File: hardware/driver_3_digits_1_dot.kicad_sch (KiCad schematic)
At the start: 12 parts, among them U4 HV5622PG

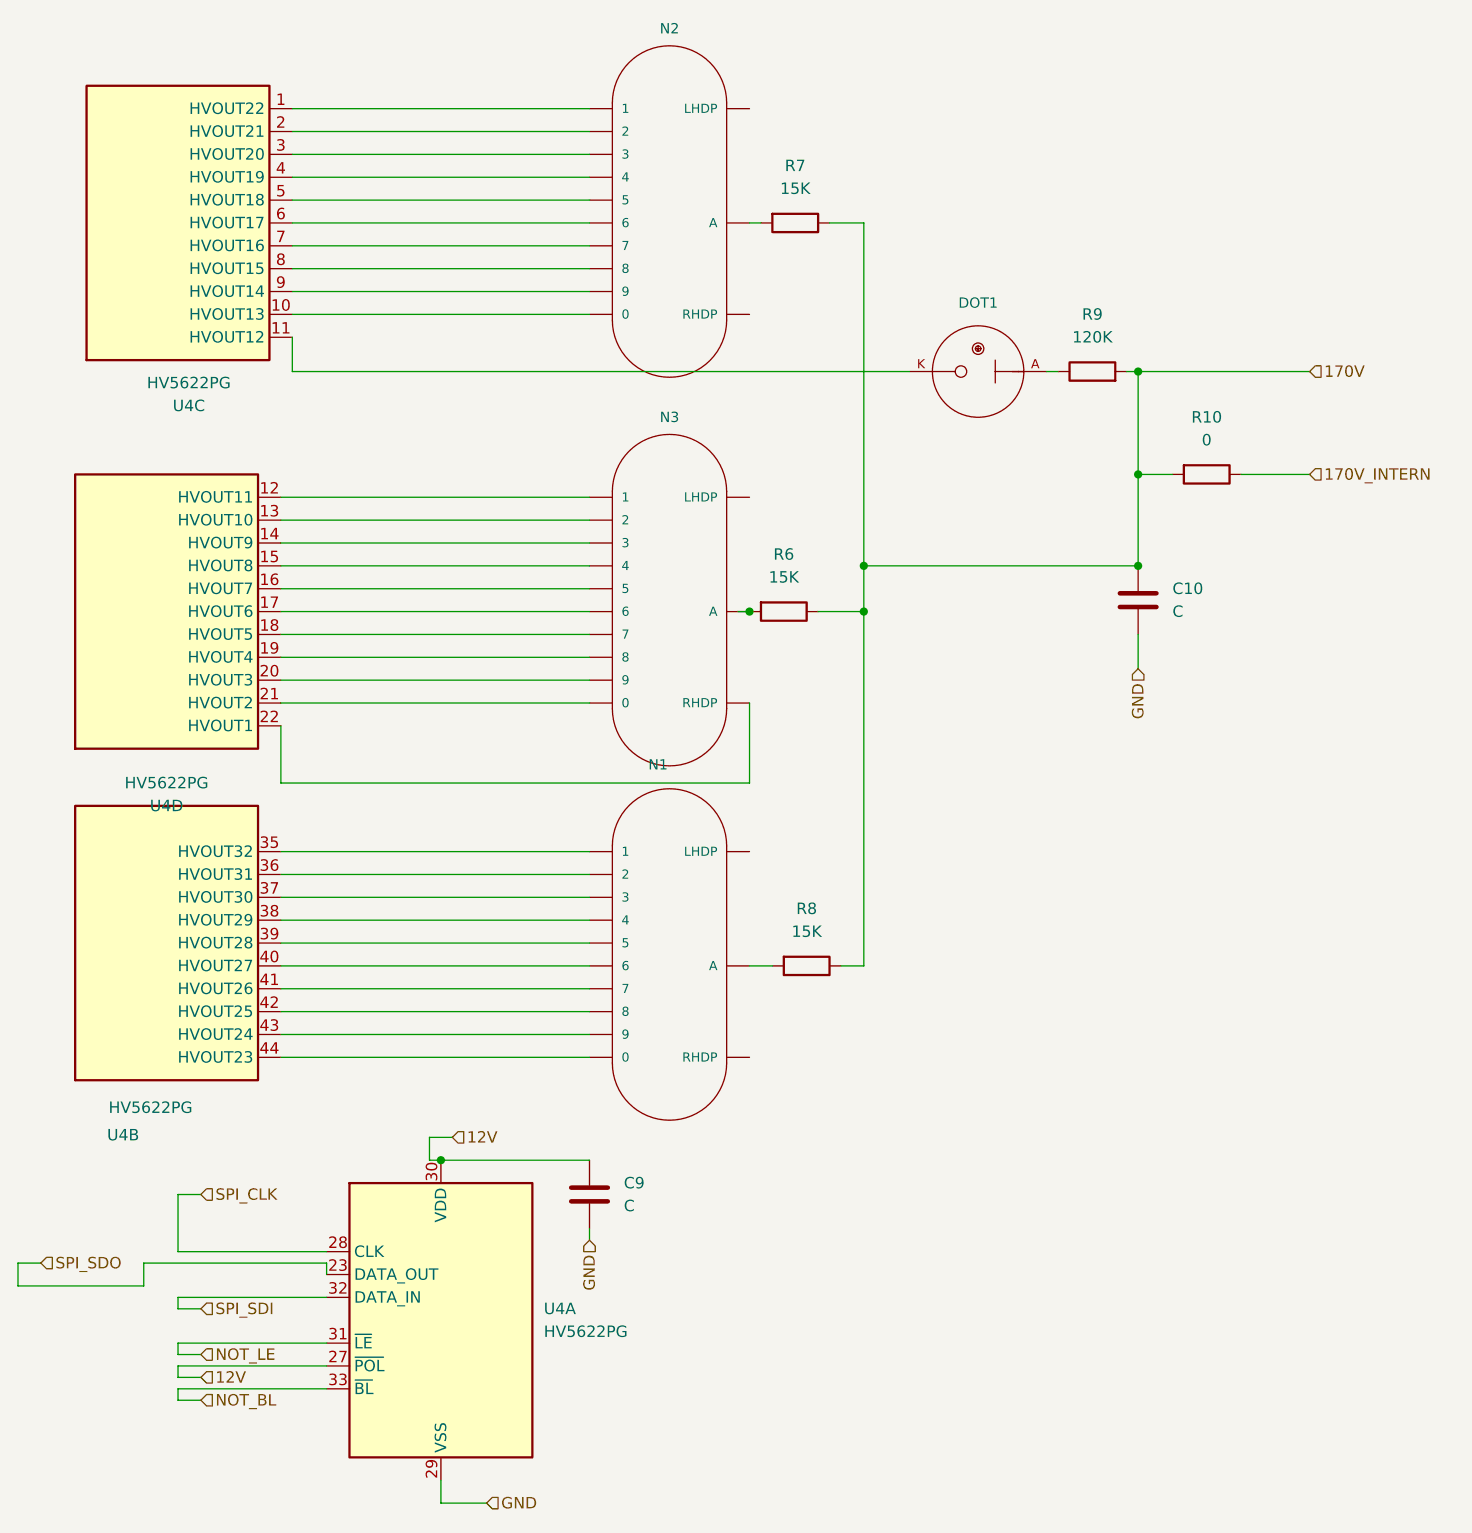
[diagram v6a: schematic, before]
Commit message: Fix most of ERC on schema. Add missing wire on RV1. Add PWR_FLG on GND to avoid error. Add resistor for unused SPI_OUT of HV5622. Add PTC on 3v3 supply.
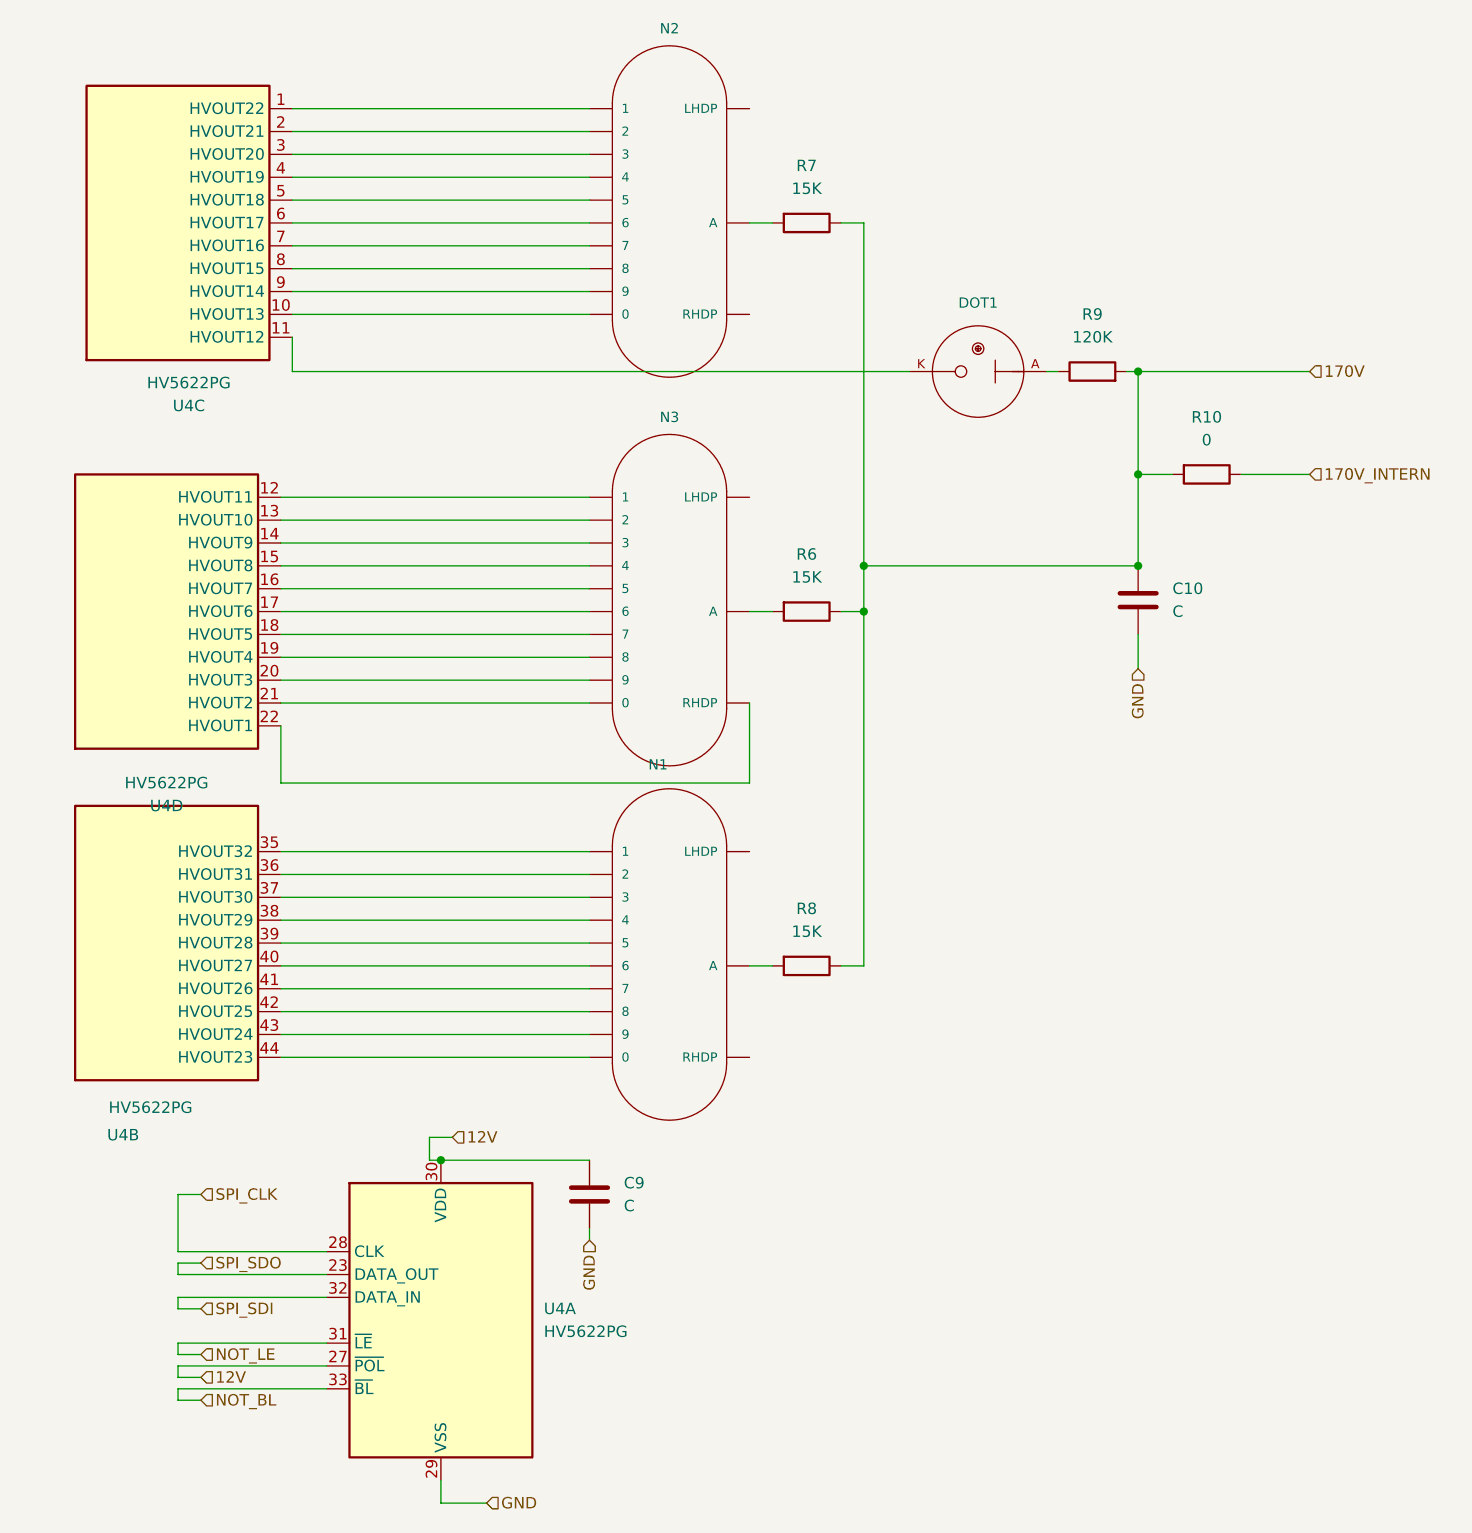
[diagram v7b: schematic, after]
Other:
- moved on the sheet: R6, R7
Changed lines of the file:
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@@
-	)
-	(junction
-		(at 139.7 87.63)
-		(diameter 0)
-		(color 0 0 0 0)
 	)
 	(junction
@@
 	(wire
 		(pts
-			(xy 148.59 44.45) (xy 152.4 44.45)
+			(xy 149.86 44.45) (xy 152.4 44.45)
 		)
 		(stroke
@@
 	(wire
 		(pts
-			(xy 72.39 162.56) (xy 58.42 162.56)
+			(xy 76.2 161.29) (xy 92.71 161.29)
 		)
 		(stroke
@@
 	(wire
 		(pts
-			(xy 139.7 44.45) (xy 140.97 44.45)
+			(xy 139.7 44.45) (xy 142.24 44.45)
 		)
 		(stroke
@@
 	(wire
 		(pts
-			(xy 147.32 87.63) (xy 152.4 87.63)
+			(xy 149.86 87.63) (xy 152.4 87.63)
 		)
 		(stroke
@@
 	(wire
 		(pts
-			(xy 92.71 161.29) (xy 92.71 160.02)
-		)
-		(stroke
-			(width 0)
-			(type default)
-		)
-	)
-	(wire
-		(pts
 			(xy 182.88 60.96) (xy 201.93 60.96)
 		)
@@
 	(wire
 		(pts
-			(xy 92.71 160.02) (xy 72.39 160.02)
-		)
-		(stroke
-			(width 0)
-			(type default)
-		)
-	)
-	(wire
-		(pts
 			(xy 88.9 52.07) (xy 121.92 52.07)
 		)
@@
 	(wire
 		(pts
+			(xy 139.7 87.63) (xy 142.24 87.63)
+		)
+		(stroke
+			(width 0)
+			(type default)
+		)
+	)
+	(wire
+		(pts
 			(xy 92.71 168.91) (xy 76.2 168.91)
 		)
@@
 	(wire
 		(pts
-			(xy 58.42 160.02) (xy 60.96 160.02)
+			(xy 76.2 160.02) (xy 78.74 160.02)
 		)
 		(stroke
@@
 	(wire
 		(pts
-			(xy 72.39 160.02) (xy 72.39 162.56)
-		)
-		(stroke
-			(width 0)
-			(type default)
-		)
-	)
-	(wire
-		(pts
 			(xy 87.63 87.63) (xy 121.92 87.63)
 		)
@@
 	(wire
 		(pts
-			(xy 58.42 162.56) (xy 58.42 160.02)
+			(xy 76.2 161.29) (xy 76.2 160.02)
 		)
 		(stroke
@@
 		(pts
 			(xy 172.72 60.96) (xy 173.99 60.96)
-		)
-		(stroke
-			(width 0)
-			(type default)
-		)
-	)
-	(wire
-		(pts
-			(xy 139.7 87.63) (xy 138.43 87.63)
 		)
 		(stroke
@@
 	(hierarchical_label "SPI_SDO"
 		(shape input)
-		(at 60.96 160.02 0)
+		(at 78.74 160.02 0)
 		(effects
 			(font
@@
 	(symbol
 		(lib_id "Device:R")
-		(at 144.78 44.45 270)
+		(at 146.05 44.45 270)
 		(unit 1)
 		(exclude_from_sim no)
@@
 		(fields_autoplaced yes)
 		(property "Reference" "R7"
-			(at 144.78 38.1 90)
+			(at 146.05 38.1 90)
 			(effects
 				(font
@@
 		)
 		(property "Value" "15K"
-			(at 144.78 40.64 90)
+			(at 146.05 40.64 90)
 			(effects
 				(font
@@
 		)
 		(property "Footprint" "Resistor_SMD:R_1206_3216Metric"
-			(at 144.78 42.672 90)
+			(at 146.05 42.672 90)
 			(effects
 				(font
@@
 		)
 		(property "Datasheet" "~"
-			(at 144.78 44.45 0)
+			(at 146.05 44.45 0)
 			(effects
 				(font
@@
 		)
 		(property "Description" "Resistor"
-			(at 144.78 44.45 0)
+			(at 146.05 44.45 0)
 			(effects
 				(font
@@
 	(symbol
 		(lib_id "Device:R")
-		(at 143.51 87.63 270)
+		(at 146.05 87.63 270)
 		(unit 1)
 		(exclude_from_sim no)
@@
 		(fields_autoplaced yes)
 		(property "Reference" "R6"
-			(at 143.51 81.28 90)
+			(at 146.05 81.28 90)
 			(effects
 				(font
@@
 		)
 		(property "Value" "15K"
-			(at 143.51 83.82 90)
+			(at 146.05 83.82 90)
 			(effects
 				(font
@@
 		)
 		(property "Footprint" "Resistor_SMD:R_1206_3216Metric"
-			(at 143.51 85.852 90)
+			(at 146.05 85.852 90)
 			(effects
 				(font
@@
 		)
 		(property "Datasheet" "~"
-			(at 143.51 87.63 0)
+			(at 146.05 87.63 0)
 			(effects
 				(font
@@
 		)
 		(property "Description" "Resistor"
-			(at 143.51 87.63 0)
-			(effects
-				(font
+			(at 146.05 87.63 0)
+			(effects
+				(font
